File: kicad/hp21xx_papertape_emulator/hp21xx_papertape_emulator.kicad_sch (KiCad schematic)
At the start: 169 parts, among them J1 SWD, J2 SERIAL, J3 Micro_SD_Card_Det_Hirose_DM3AT, J5 Conn_02x13_Odd_Even, Q1 2N7002, Q10 2N7002, Q11 2N7002, Q12 BSS84, Q13 2N7002, Q14 2N7002, Q15 BSS84, Q2 2N7002, Q3 2N7002, Q4 2N7002, Q5 2N7002, Q6 2N7002, Q7 2N7002, Q8 2N7002, Q9 2N7002, SW1 Select, SW2 Up, SW3 Down, U1 TLV75533PDRV, U2 STM32F103C8Tx, U3 USBLC6-2SC6, U4 AP3012, U6 74LVC14, U7 74LVC245, Y1 8MHz

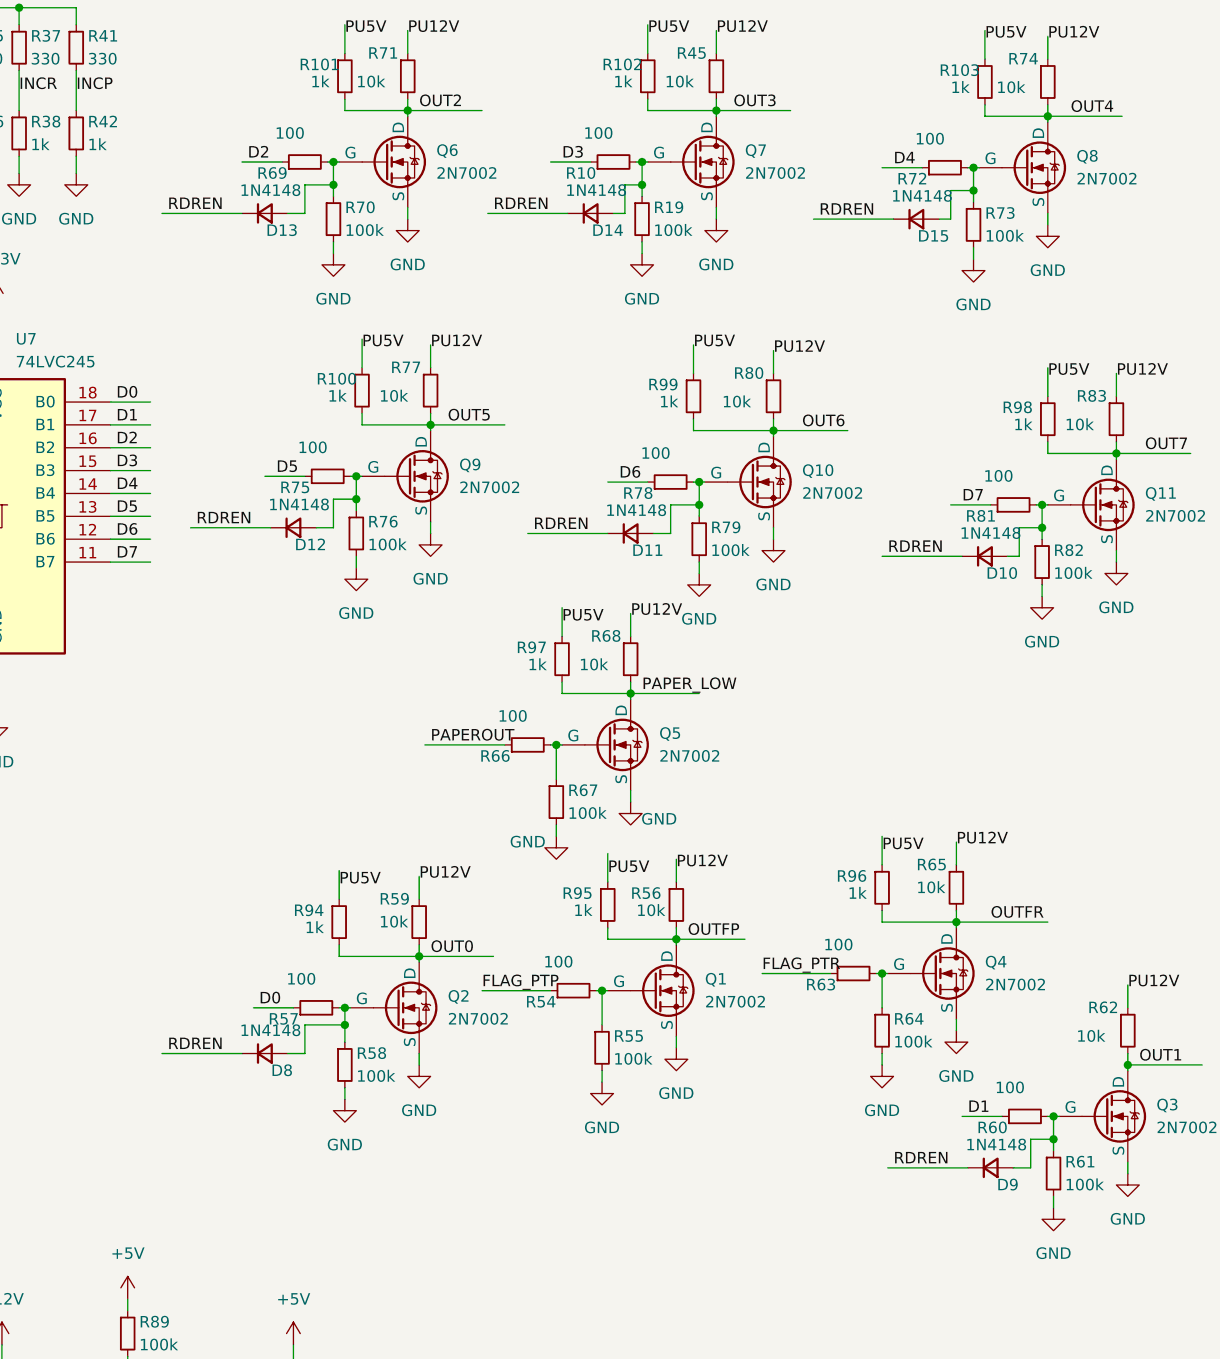
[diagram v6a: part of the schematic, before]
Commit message: Removed the enable function since it wasn't a good idea.
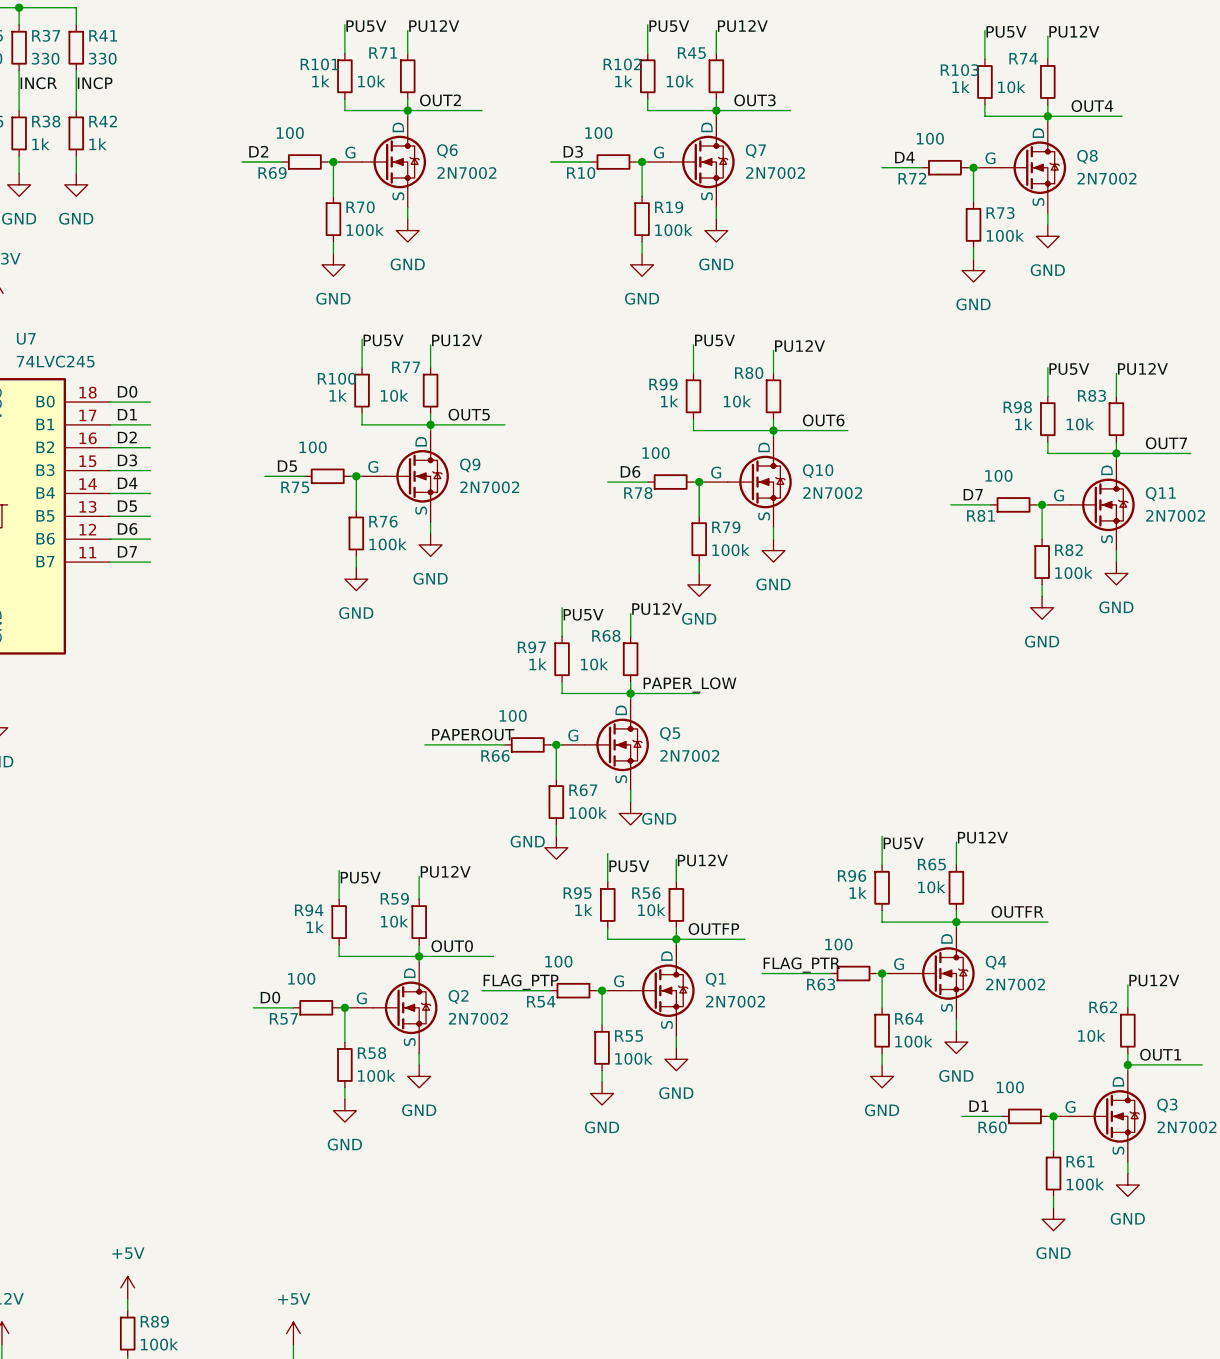
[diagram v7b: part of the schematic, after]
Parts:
- removed D10, D11, D12, D13, D14, D15, D8, D9: 1N4148, Diode_SMD:D_SOD-323, symbol Device:D_Small

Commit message: New drivers.
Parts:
- removed R47, R48, R49, R50, R51, R52, R53: 22, Resistor_SMD:R_0402_1005Metric, symbol Device:R_Small
- Q12, Q15: footprint (none) -> Package_TO_SOT_SMD:SOT-23
- R46: value 22 -> 1k; LCSC C25092 -> C11702
- U4: LCSC (none) -> C102618
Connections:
- net OUT0: now also J5.24 (Pin_24)
- net OUT1: now also J5.23 (Pin_23), R46.2
- net OUT2: now also J5.22 (Pin_22)
- net OUT3: now also J5.21 (Pin_21)
- net OUT4: now also J5.20 (Pin_20)
- net OUT5: now also J5.19 (Pin_19)
- net OUT6: now also J5.18 (Pin_18); no longer R46.2
- net OUT7: now also J5.17 (Pin_17)
- net PU5V: now also R46.1
- net RDREN: no longer names the net of U2.46 (PB9)
- no-connect marks 10 -> 11
